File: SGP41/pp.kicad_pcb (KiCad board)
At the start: 2 copper layers, 12.1 x 23.5 mm, 11 parts, among them J1 Conn_01x03, J2 Conn_01x04, U2 CH32V003AxMx, U3 AP62250WU-7

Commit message: SGP41 from sensirion - start work!
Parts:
- removed U2: CH32V003AxMx, Package_SO:SOP-16_3.9x9.9mm_P1.27mm
- added C4: 1uF, Capacitor_SMD:C_0805_2012Metric, F.Cu at (116.0, 72.0)
- added C5: C_Small, Capacitor_SMD:C_0805_2012Metric, F.Cu at (122.5, 75.7)
- added R3: 4.7, Resistor_SMD:R_0805_2012Metric, F.Cu at (115.9, 75.6)
- added R4: R_Small, Resistor_SMD:R_0805_2012Metric, F.Cu at (122.5, 71.9)
- added R5: R_Small, Resistor_SMD:R_0805_2012Metric, F.Cu at (119.3, 74.7)
- added U1: SGP41-D-R4, asd:DFN_SGP41-D-R4_SEN, F.Cu at (119.3, 71.8)
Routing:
- net +5V: track 23.6 -> 51.5 mm, vias 0 -> 1
- net /SWIO: track 14.0 -> 0.00 mm
- net /Grove1: track 10.5 -> 0.00 mm
- net /Grove2: track 9.72 -> 0.00 mm
- net +3V3: track 11.9 -> 6.60 mm, vias 1 -> 0
- net Net-(U1-VDD): track 0.00 -> 4.86 mm
- net Net-(U1-SDA): track 0.00 -> 2.22 mm
- net Net-(U1-SCL): track 0.00 -> 2.01 mm

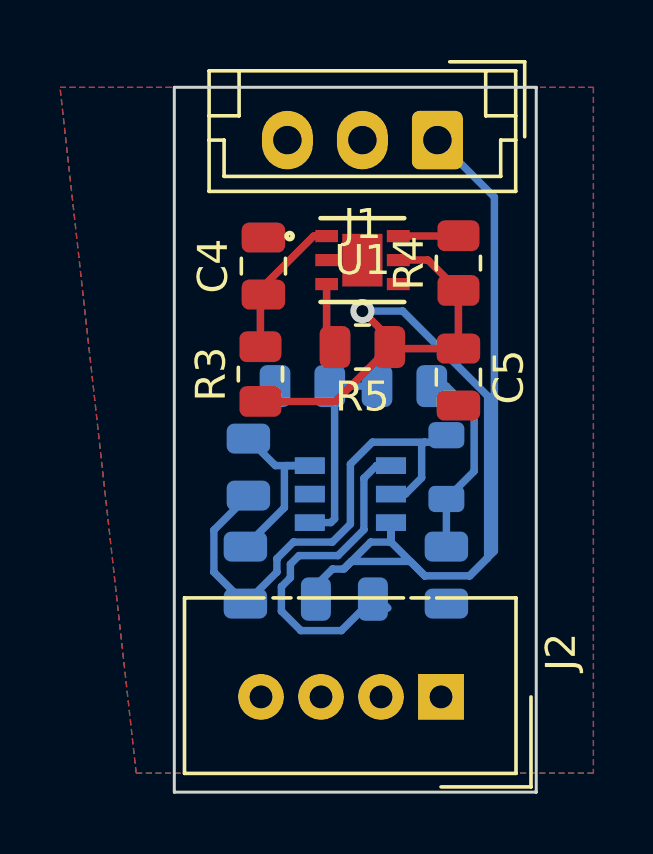
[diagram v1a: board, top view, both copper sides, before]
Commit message: Swap over to STM32 controller
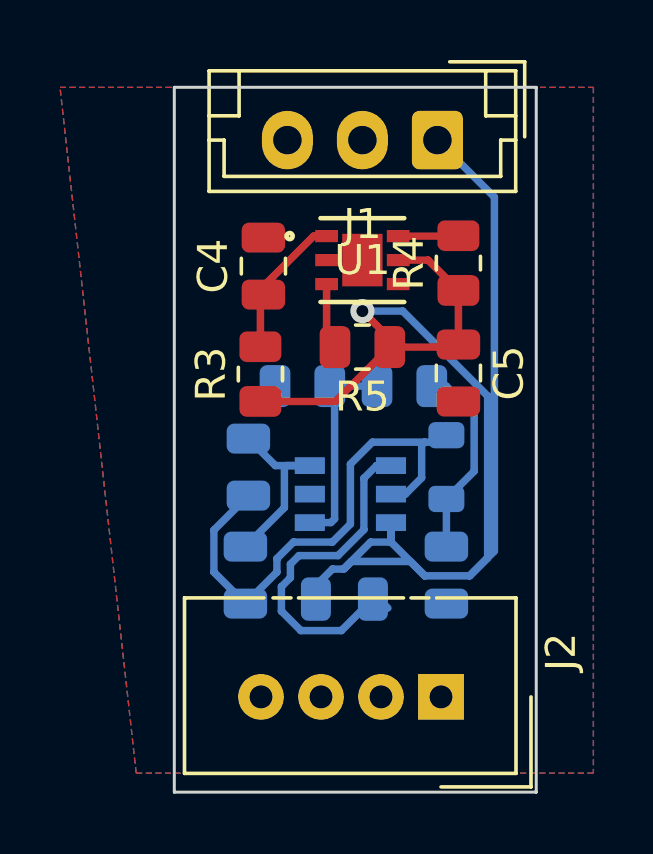
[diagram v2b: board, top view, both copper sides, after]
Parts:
- moved C5 0.14 mm to (122.5, 75.6)
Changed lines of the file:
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@@
 		(tags "resistor")
 		(property "Reference" "R3"
-			(at 0 -1.65 270)
+			(at 0 -1.65 -90)
 			(layer "F.SilkS")
 			(effects
@@
 		)
 		(property "Value" "4.7"
-			(at 0 1.65 270)
+			(at 0 1.65 -90)
 			(layer "F.Fab")
 			(effects
@@
 				(font
 					(size 1.27 1.27)
+					(thickness 0.15)
 				)
 			)
@@
 				(font
 					(size 1.27 1.27)
+					(thickness 0.15)
 				)
 			)
@@
 				(font
 					(size 1.27 1.27)
+					(thickness 0.15)
 				)
 			)
@@
 		)
 		(fp_text user "${REFERENCE}"
-			(at 0 0 270)
+			(at 0 0 -90)
 			(layer "F.Fab")
 			(effects
@@
 		(tags "resistor")
 		(property "Reference" "R4"
-			(at 0 -1.65 270)
+			(at 0 -1.65 -90)
 			(layer "F.SilkS")
 			(effects
@@
 		)
 		(property "Value" "R_Small"
-			(at 0 1.65 270)
+			(at 0 1.65 -90)
 			(layer "F.Fab")
 			(effects
@@
 				(font
 					(size 1.27 1.27)
+					(thickness 0.15)
 				)
 			)
@@
 				(font
 					(size 1.27 1.27)
+					(thickness 0.15)
 				)
 			)
@@
 				(font
 					(size 1.27 1.27)
+					(thickness 0.15)
 				)
 			)
@@
 		)
 		(fp_text user "${REFERENCE}"
-			(at 0 0 270)
+			(at 0 0 -90)
 			(layer "F.Fab")
 			(effects
@@
 	(footprint "Capacitor_SMD:C_0805_2012Metric"
 		(layer "F.Cu")
-		(at 122.5 75.7 -90)
+		(at 122.5 75.565 -90)
 		(descr "Capacitor SMD 0805 (2012 Metric), square (rectangular) end terminal, IPC_7351 nominal, (Body size source: IPC-SM-782 page 76, https://www.pcb-3d.com/wordpress/wp-content/uploads/ipc-sm-782a_amendment_1_and_2.pdf, https://docs.google.com/spreadsheets/d/1BsfQQcO9C6DZCsRaXUlFlo91Tg2WpOkGARC1WS5S8t0/edit?usp=sharing), generated with kicad-footprint-generator")
 		(tags "capacitor")
@@
 				(font
 					(size 1.27 1.27)
+					(thickness 0.15)
 				)
 			)
@@
 				(font
 					(size 1.27 1.27)
+					(thickness 0.15)
 				)
 			)
@@
 				(font
 					(size 1.27 1.27)
+					(thickness 0.15)
 				)
 			)
@@
 				(font
 					(size 1.27 1.27)
+					(thickness 0.15)
 				)
 			)
@@
 				(font
 					(size 1.27 1.27)
+					(thickness 0.15)
 				)
 			)
@@
 				(font
 					(size 1.27 1.27)
+					(thickness 0.15)
 				)
 			)
@@
 				(font
 					(size 1.27 1.27)
+					(thickness 0.15)
 				)
 			)
@@
 				(font
 					(size 1.27 1.27)
+					(thickness 0.15)
 				)
 			)
@@
 				(font
 					(size 1.27 1.27)
+					(thickness 0.15)
 				)
 			)
@@
 		(tags "capacitor")
 		(property "Reference" "C4"
-			(at 0 -1.68 270)
+			(at 0 -1.68 -90)
 			(layer "F.SilkS")
 			(effects
@@
 		)
 		(property "Value" "1uF"
-			(at 0 1.68 270)
+			(at 0 1.68 -90)
 			(layer "F.Fab")
 			(effects
@@
 				(font
 					(size 1.27 1.27)
+					(thickness 0.15)
 				)
 			)
@@
 				(font
 					(size 1.27 1.27)
+					(thickness 0.15)
 				)
 			)
@@
 				(font
 					(size 1.27 1.27)
+					(thickness 0.15)
 				)
 			)
@@
 		)
 		(fp_text user "${REFERENCE}"
-			(at 0 0 270)
+			(at 0 0 -90)
 			(layer "F.Fab")
 			(effects
@@
 				(font
 					(size 1.27 1.27)
+					(thickness 0.15)
 				)
 			)
@@
 				(font
 					(size 1.27 1.27)
+					(thickness 0.15)
 				)
 			)
@@
 				(font
 					(size 1.27 1.27)
+					(thickness 0.15)
 				)
 			)
@@
 				(font
 					(size 1.27 1.27)
+					(thickness 0.15)
 				)
 			)
@@
 				(font
 					(size 1.27 1.27)
+					(thickness 0.15)
 				)
 			)
@@
 				(font
 					(size 1.27 1.27)
+					(thickness 0.15)
 				)
 			)
@@
 				(font
 					(size 1.27 1.27)
+					(thickness 0.15)
 				)
 				(justify mirror)
@@
 				(font
 					(size 1.27 1.27)
+					(thickness 0.15)
 				)
 				(justify mirror)
@@
 				(font
 					(size 1.27 1.27)
+					(thickness 0.15)
 				)
 				(justify mirror)
@@
 				(font
 					(size 1.27 1.27)
+					(thickness 0.15)
 				)
 			)
@@
 				(font
 					(size 1.27 1.27)
+					(thickness 0.15)
 				)
 			)
@@
 				(font
 					(size 1.27 1.27)
+					(thickness 0.15)
 				)
 			)
@@
 				(font
 					(size 1.27 1.27)
+					(thickness 0.15)
 				)
 			)
@@
 				(font
 					(size 1.27 1.27)
+					(thickness 0.15)
 				)
 			)
@@
 				(font
 					(size 1.27 1.27)
+					(thickness 0.15)
 				)
 			)
@@
 				(font
 					(size 1.27 1.27)
+					(thickness 0.15)
 				)
 				(justify mirror)
@@
 				(font
 					(size 1.27 1.27)
+					(thickness 0.15)
 				)
 				(justify mirror)
@@
 				(font
 					(size 1.27 1.27)
+					(thickness 0.15)
 				)
 				(justify mirror)
@@
 				(font
 					(size 1.27 1.27)
+					(thickness 0.15)
 				)
 			)
@@
 				(font
 					(size 1.27 1.27)
+					(thickness 0.15)
 				)
 			)
@@
 				(font
 					(size 1.27 1.27)
+					(thickness 0.15)
 				)
 			)
@@
 				(font
 					(size 1.27 1.27)
+					(thickness 0.15)
 				)
 			)
@@
 				(font
 					(size 1.27 1.27)
+					(thickness 0.15)
 				)
 			)
@@
 				(font
 					(size 1.27 1.27)
+					(thickness 0.15)
 				)
 			)
@@
 				(font
 					(size 1.27 1.27)
+					(thickness 0.15)
 				)
 			)
@@
 				(font
 					(size 1.27 1.27)
+					(thickness 0.15)
 				)
 			)
@@
 				(font
 					(size 1.27 1.27)
+					(thickness 0.15)
 				)
 			)
@@
 				(font
 					(size 1.27 1.27)
+					(thickness 0.15)
 				)
 			)
@@
 				(font
 					(size 1.27 1.27)
+					(thickness 0.15)
 				)
 			)
@@
 				(font
 					(size 1.27 1.27)
+					(thickness 0.15)
 				)
 			)
@@
 	(segment
 		(start 122.5 72.8125)
-		(end 122.5 74.75)
-		(width 0.25)
-		(layer "F.Cu")
-		(net 2)
-	)
-	(segment
-		(start 122.5 74.75)
-		(end 120.2625 74.75)
+		(end 122.5 74.615)
 		(width 0.25)
 		(layer "F.Cu")
@@
 	)
 	(segment
-		(start 118.4 76.5125)
+		(start 122.415 74.7)
 		(end 120.2125 74.7)
 		(width 0.25)
@@
 	)
 	(segment
-		(start 120.2625 74.75)
+		(start 118.4 76.5125)
 		(end 120.2125 74.7)
 		(width 0.25)
 		(layer "F.Cu")
+		(net 2)
+	)
+	(segment
+		(start 122.5 74.615)
+		(end 122.415 74.7)
+		(width 0.25)
+		(layer "F.Cu")
